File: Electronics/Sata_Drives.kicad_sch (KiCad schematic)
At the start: 66 parts

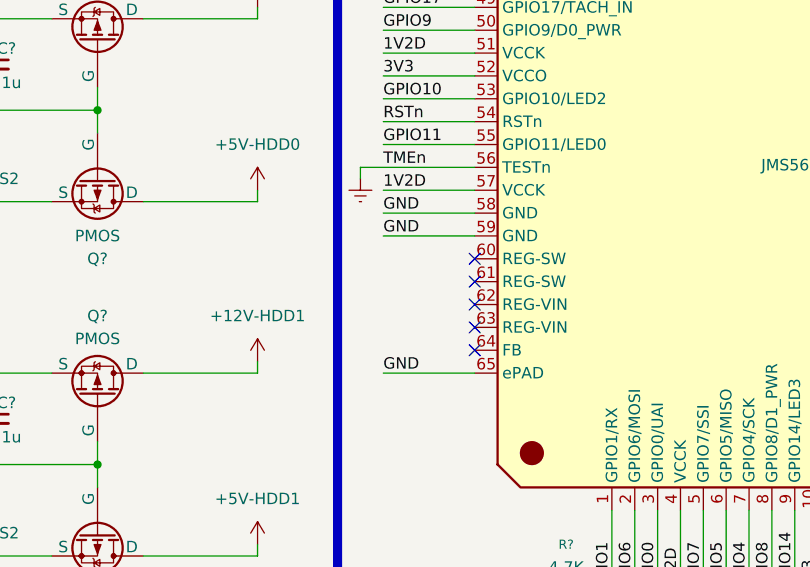
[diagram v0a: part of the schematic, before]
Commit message: RP2040 Added, Files Structure Changed
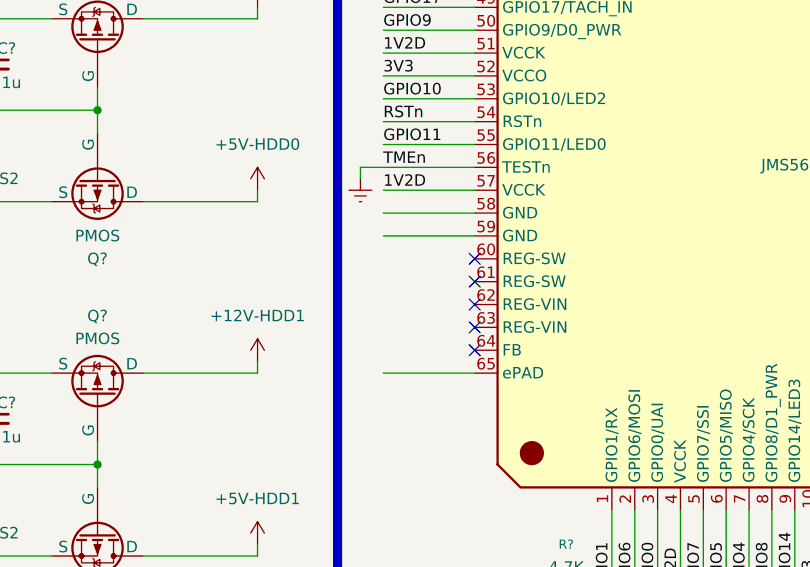
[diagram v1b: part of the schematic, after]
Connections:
- net GND: no longer names the net of U?.58 (GND), U?.59 (GND), U?.65 (ePAD)
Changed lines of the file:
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@@
 		)
 	)
-	(label "GND"
+	(label ""
 		(at 105.41 74.93 0)
 		(effects
@@
 		)
 	)
-	(label "GND"
+	(label ""
 		(at 105.41 90.17 0)
 		(effects
@@
 		)
 	)
-	(label "GND"
+	(label ""
 		(at 105.41 72.39 0)
 		(effects

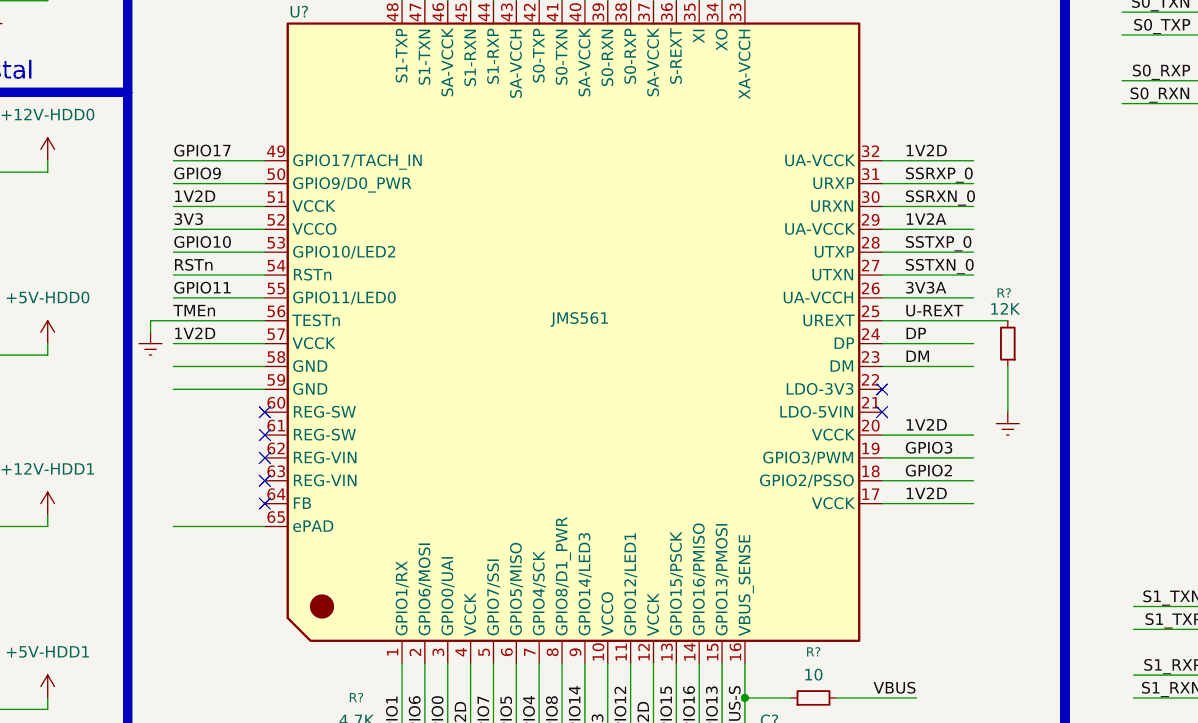
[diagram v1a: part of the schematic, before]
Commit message: Rp2040 Power Sequence finished and general cleaning
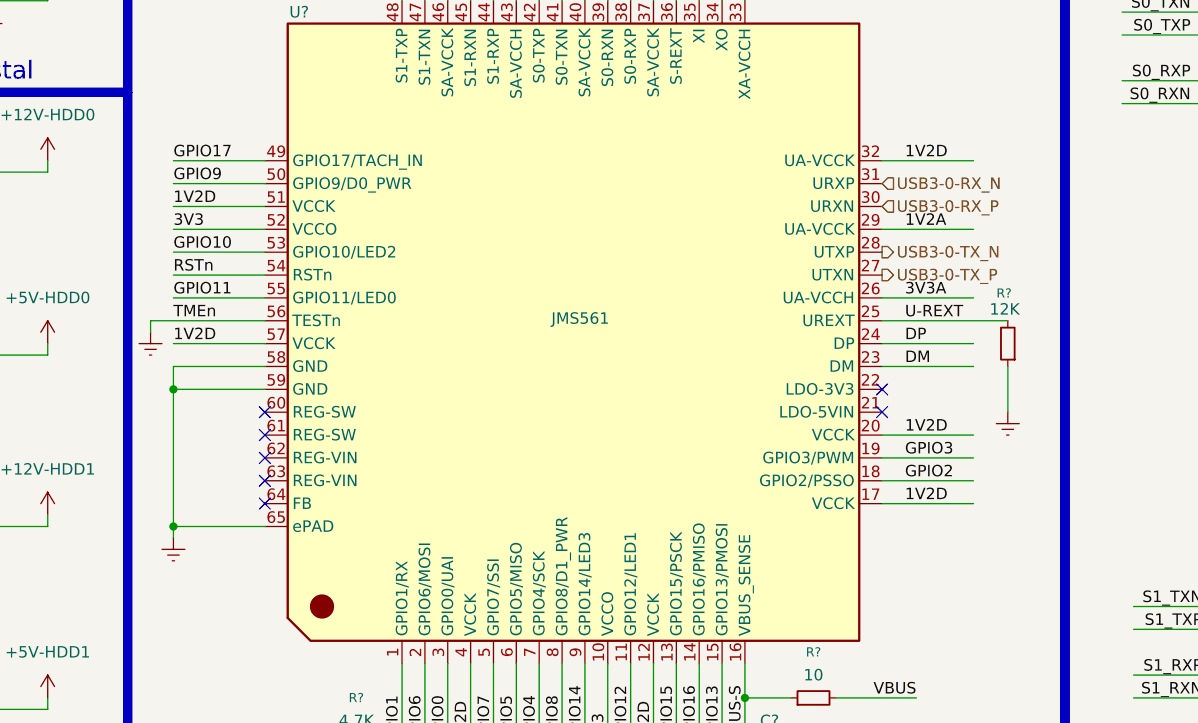
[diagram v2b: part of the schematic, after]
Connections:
- net SSRXN_0 renamed USB3-0-RX_P
- net SSRXP_0 renamed USB3-0-RX_N
- net SSTXN_0 renamed USB3-0-TX_P
- net SSTXP_0 renamed USB3-0-TX_N
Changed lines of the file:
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@@
 	)
 	(junction
+		(at 105.41 90.17)
+		(diameter 0)
+		(color 0 0 0 0)
+	)
+	(junction
 		(at 229.87 104.14)
 		(diameter 0)
@@
 	)
 	(junction
+		(at 105.41 74.93)
+		(diameter 0)
+		(color 0 0 0 0)
+	)
+	(junction
 		(at 29.21 163.83)
 		(diameter 0)
@@
 	(wire
 		(pts
+			(xy 105.41 90.17) (xy 105.41 91.44)
+		)
+		(stroke
+			(width 0)
+			(type default)
+		)
+	)
+	(wire
+		(pts
 			(xy 231.14 30.48) (xy 229.87 30.48)
 		)
@@
 	(wire
 		(pts
+			(xy 105.41 72.39) (xy 105.41 74.93)
+		)
+		(stroke
+			(width 0)
+			(type default)
+		)
+	)
+	(wire
+		(pts
 			(xy 273.05 127) (xy 280.67 127)
 		)
@@
 	(wire
 		(pts
-			(xy 184.15 59.69) (xy 194.31 59.69)
-		)
-		(stroke
-			(width 0)
-			(type default)
-		)
-	)
-	(wire
-		(pts
 			(xy 262.89 121.92) (xy 262.89 124.46)
 		)
@@
 	(wire
 		(pts
-			(xy 184.15 62.23) (xy 194.31 62.23)
-		)
-		(stroke
-			(width 0)
-			(type default)
-		)
-	)
-	(wire
-		(pts
 			(xy 264.16 129.54) (xy 264.16 127)
 		)
@@
 	(wire
 		(pts
-			(xy 184.15 52.07) (xy 194.31 52.07)
-		)
-		(stroke
-			(width 0)
-			(type default)
-		)
-	)
-	(wire
-		(pts
 			(xy 24.13 15.24) (xy 34.29 15.24)
 		)
@@
 	(wire
 		(pts
-			(xy 184.15 54.61) (xy 194.31 54.61)
-		)
-		(stroke
-			(width 0)
-			(type default)
-		)
-	)
-	(wire
-		(pts
 			(xy 130.81 146.05) (xy 134.62 146.05)
 		)
@@
 	(wire
 		(pts
+			(xy 105.41 74.93) (xy 105.41 90.17)
+		)
+		(stroke
+			(width 0)
+			(type default)
+		)
+	)
+	(wire
+		(pts
 			(xy 144.78 146.05) (xy 139.7 146.05)
 		)
@@
 		)
 	)
-	(label "SSRXN_0"
-		(at 186.69 54.61 0)
-		(effects
-			(font
-				(size 1.27 1.27)
-			)
-			(justify left bottom)
-		)
-	)
 	(label "GPIO9"
 		(at 21.59 67.31 180)
@@
 		)
 	)
-	(label "SSTXN_0"
-		(at 186.69 62.23 0)
-		(effects
-			(font
-				(size 1.27 1.27)
-			)
-			(justify left bottom)
-		)
-	)
 	(label "GPIO1"
 		(at 130.81 114.3 90)
@@
 		)
 	)
-	(label "SSRXP_0"
-		(at 186.69 52.07 0)
-		(effects
-			(font
-				(size 1.27 1.27)
-			)
-			(justify left bottom)
-		)
-	)
 	(label "GPIO0"
 		(at 135.89 114.3 90)
@@
 		)
 	)
-	(label "SSTXP_0"
-		(at 186.69 59.69 0)
-		(effects
-			(font
-				(size 1.27 1.27)
-			)
-			(justify left bottom)
-		)
-	)
 	(label "GPIO9"
 		(at 105.41 52.07 0)
@@
 		)
 	)
+	(hierarchical_label "USB3-0-TX_N"
+		(shape output)
+		(at 184.15 59.69 0)
+		(effects
+			(font
+				(size 1.27 1.27)
+			)
+			(justify left)
+		)
+	)
+	(hierarchical_label "USB3-0-TX_P"
+		(shape output)
+		(at 184.15 62.23 0)
+		(effects
+			(font
+				(size 1.27 1.27)
+			)
+			(justify left)
+		)
+	)
 	(hierarchical_label "+3V3A"
 		(shape input)
@@
 		)
 	)
+	(hierarchical_label "USB3-0-RX_P"
+		(shape input)
+		(at 184.15 54.61 0)
+		(effects
+			(font
+				(size 1.27 1.27)
+			)
+			(justify left)
+		)
+	)
 	(hierarchical_label "+1V2"
 		(shape input)
@@
 		)
 	)
+	(hierarchical_label "USB3-0-RX_N"
+		(shape input)
+		(at 184.15 52.07 0)
+		(effects
+			(font
+				(size 1.27 1.27)
+			)
+			(justify left)
+		)
+	)
 	(symbol
 		(lib_id "Device:R_Small")
@@
 					(unit 1)
 				)
+			)
+		)
+	)
+	(symbol
+		(lib_id "power:Earth")
+		(at 105.41 91.44 0)
+		(unit 1)
+		(exclude_from_sim no)
+		(in_bom yes)
+		(on_board yes)
+		(dnp no)
+		(property "Reference" "#PWR0162"
+			(at 105.41 97.79 0)
+			(effects
+				(font
+					(size 1.27 1.27)
+				)
+				(hide yes)
+			)
+		)
+		(property "Value" "~"
+			(at 105.41 95.25 0)
+			(effects
+				(font
+					(size 1.27 1.27)
+				)
+			)
+		)
+		(property "Footprint" ""
+			(at 105.41 91.44 0)
+			(effects
+				(font
+					(size 1.27 1.27)
+				)
+				(hide yes)
+			)
+		)
+		(property "Datasheet" "~"
+			(at 105.41 91.44 0)
+			(effects
+				(font
+					(size 1.27 1.27)
+				)
+				(hide yes)
+			)
+		)
+		(property "Description" "Power symbol creates a global label with name \"Earth\""
+			(at 105.41 91.44 0)
+			(effects
+				(font
+					(size 1.27 1.27)
+				)
+				(hide yes)
+			)
+		)
+		(pin "1"
+		)
+		(instances
+			(project "CM5 Nas"
+				(path "/0650c7a8-acba-429c-9f8e-eec0baf0bc1c/fede4c36-00cc-4d3d-b71c-5243ba232202/a72edad3-d792-4f36-af8a-632fcfbc9d26"
+					(reference "#PWR0162")
+					(unit 1)
+				)

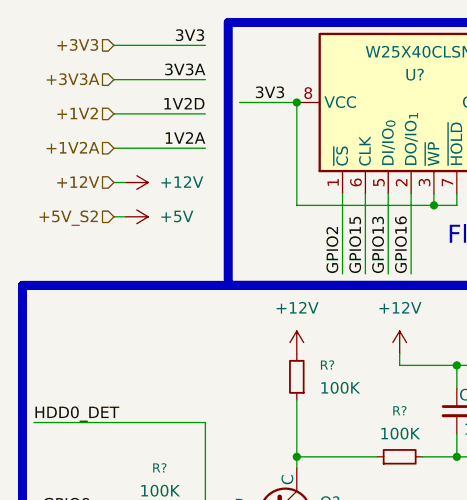
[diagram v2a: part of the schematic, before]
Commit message: Starting the Sheet connections
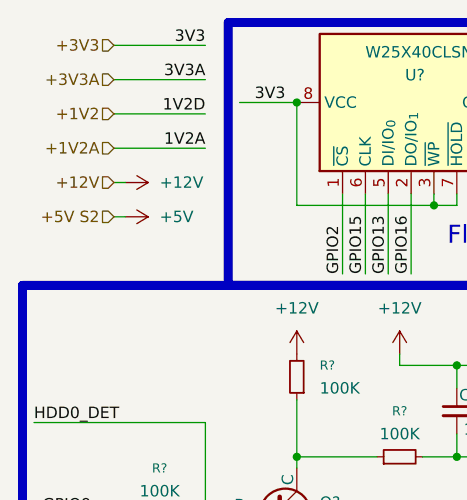
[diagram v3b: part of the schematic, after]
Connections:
- net +5V S2 is gone; now on net +5V: Q?.3 (S), Q?.3 (S), R?.1, R?.1
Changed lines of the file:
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@@
 		)
 	)
-	(hierarchical_label "+5V_S2"
+	(hierarchical_label "+5V S2"
 		(shape input)
 		(at 24.13 34.29 180)

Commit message: Footprints Selected
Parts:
- removed D? (x4): LED_Small, symbol Device:LED_Small
- removed Y?: 30MHz, symbol Device:Crystal
- added D16, D17, D18, D19: LED Green, LED_SMD:LED_0603_1608Metric, symbol Device:LED
- added Y1: 30MHz, ABM8-30.000MHZ-B2-T:ABM810000MHZ12D2W, symbol Device:Crystal_GND24
- C100, C101, C102, C103, C104, C105, C106, C107, C108, C109, C110, C111, C112, C113, C114, C115, C116, C117, C89, C90, C91, C92, C93, C94, C95, C96, C97, C98, C99: renamed from C?; footprint (none) -> Capacitor_SMD:C_0603_1608Metric
- JP2, JP3: renamed from JP?; footprint (none) -> Connector_PinHeader_2.54mm:PinHeader_1x03_P2.54mm_Vertical
- Q10, Q11, Q4, Q5: renamed from Q?; footprint (none) -> MMBT3904:P200_SOT-23
- Q6, Q7, Q8, Q9: renamed from Q?; footprint (none) -> AOSS21311C:SOT95P237X117-3N
- R50, R51, R52, R53, R54, R55, R56, R57, R63, R64, R65, R66, R67: renamed from R?; footprint (none) -> Resistor_SMD:R_0603_1608Metric
- R58: renamed from R?; value 4.7K -> 4.7K 1%; footprint (none) -> Resistor_SMD:R_0603_1608Metric
- R59, R60, R61, R62: renamed from R?; value 330 -> 1k; footprint (none) -> Resistor_SMD:R_0603_1608Metric
- gave numbers to parts that had none: 4
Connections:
- net XIN: now also Y1.1
- net XOUT: now also Y1.3
- net at R62.2: now also D19.2 (A)
- net at R61.2: now also D18.2 (A)
- net at R60.2: now also D17.2 (A)
- net at C103.2, C104.2: now also Y1.4
- net at R59.2: now also D16.2 (A)
- new net: D16.1 (K), D17.1 (K), D18.1 (K), D19.1 (K)

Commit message: Footprints selected, Hiracicle connections created, Pcb next
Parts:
- C100: renamed from C111; footprint Capacitor_SMD:C_0603_1608Metric -> Capacitor_SMD:C_0402_1005Metric
- C101: renamed from C112; footprint Capacitor_SMD:C_0603_1608Metric -> Capacitor_SMD:C_0402_1005Metric
- C102: renamed from C113; footprint Capacitor_SMD:C_0603_1608Metric -> Capacitor_SMD:C_0402_1005Metric
- C104: renamed from C114; footprint Capacitor_SMD:C_0603_1608Metric -> Capacitor_SMD:C_1206_3216Metric
- C105: renamed from C117; footprint Capacitor_SMD:C_0603_1608Metric -> Capacitor_SMD:C_1206_3216Metric
- C112: renamed from C95; footprint Capacitor_SMD:C_0603_1608Metric -> Capacitor_SMD:C_0805_2012Metric
- C113: renamed from C97; footprint Capacitor_SMD:C_0603_1608Metric -> Capacitor_SMD:C_0805_2012Metric
- C116: renamed from C91; footprint Capacitor_SMD:C_0603_1608Metric -> Capacitor_SMD:C_0805_2012Metric
- C89: renamed from C103; footprint Capacitor_SMD:C_0603_1608Metric -> Capacitor_SMD:C_0402_1005Metric
- C90: renamed from C104; footprint Capacitor_SMD:C_0603_1608Metric -> Capacitor_SMD:C_0402_1005Metric
- C91: renamed from C106; footprint Capacitor_SMD:C_0603_1608Metric -> Capacitor_SMD:C_0402_1005Metric
- C92: renamed from C107; footprint Capacitor_SMD:C_0603_1608Metric -> Capacitor_SMD:C_0402_1005Metric
- C93: renamed from C108; footprint Capacitor_SMD:C_0603_1608Metric -> Capacitor_SMD:C_0402_1005Metric
- C94: renamed from C109; footprint Capacitor_SMD:C_0603_1608Metric -> Capacitor_SMD:C_0402_1005Metric
- C95: renamed from C115; footprint Capacitor_SMD:C_0603_1608Metric -> Capacitor_SMD:C_1206_3216Metric
- C96: renamed from C101; footprint Capacitor_SMD:C_0603_1608Metric -> Capacitor_SMD:C_0805_2012Metric
- C97: renamed from C116; footprint Capacitor_SMD:C_0603_1608Metric -> Capacitor_SMD:C_1206_3216Metric
- C98: renamed from C102; footprint Capacitor_SMD:C_0603_1608Metric -> Capacitor_SMD:C_0805_2012Metric
- C99: renamed from C110; footprint Capacitor_SMD:C_0603_1608Metric -> Capacitor_SMD:C_0402_1005Metric
- R54: renamed from R50; value 4.7K -> 4K7
- R60: renamed from R51; value 4.7K -> 4K7
- R61: renamed from R58; value 4.7K 1% -> 4K7 1%
- R62: renamed from R59; value 1k -> 270
- R63: renamed from R60; value 1k -> 270
- R64: renamed from R61; value 1k -> 270
- R65: renamed from R62; value 1k -> 270
- renumbered C105 to C103, C89 to C106, C92 to C107, C96 to C108, C99 to C109, C90 to C110, C93 to C111, C98 to C114, C100 to C115, C94 to C117, D16 to D14, D17 to D15, D18 to D16, D19 to D17, JP2 to JP1, JP3 to JP2, Q10 to Q2, Q6 to Q3, Q7 to Q5, Q8 to Q6, Q5 to Q7, Q11 to Q8, R63 to R48, R66 to R49, R54 to R50, R56 to R51, R65 to R53, R67 to R56, R53 to R58, R64 to R59
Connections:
- net TMEn is gone; now on net gnd: U10.56 (TESTn)
- net gnd: now reaches C113.2, C114.2, C115.2
- net gnd: now also C103.2, C104.2, C105.2, C106.2, C107.2, C108.2, C109.2, C110.2, C111.2, C112.2, C116.2, C117.2, C89.2, C90.2, C95.2, C97.2, D14.1 (K), D15.1 (K), D16.1 (K), D17.1 (K), J20.P10, J20.P11, J20.P12, J20.P4, J20.P6, J20.S1, J20.S4, J20.S7, J20.SH1 (SHIELD), J20.SH2 (SHIELD), J21.P10, J21.P11, J21.P12, J21.P4, J21.P6, J21.S1, J21.S4, J21.S7, J21.SH1 (SHIELD), J21.SH2 (SHIELD), JP1.3 (B), JP2.3 (B), Q2.3 (E), Q4.3 (E), Q7.3 (E), Q8.3 (E), R48.2, R53.1, R54.2, R60.2, U10.58 (GND), U10.59 (GND), U10.65 (ePAD), U9.4 (GND), Y1.2, Y1.4
